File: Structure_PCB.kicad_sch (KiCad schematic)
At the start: 137 parts, among them J10 JST-GH 4Pin, J11 JST-GH 4Pin, J12 JST-GH 4Pin, J6 6620XX236022_662004236022, J9 Conn_02x04_Top_Bottom, K2 FINDER-40.61

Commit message: updated StructurePcB
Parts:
- removed D4, D5, D6: ~, Diode_SMD:D_SOD-123F, symbol Device:D_Schottky
- removed F1: 100 mA, Fuse:Fuse_1206_3216Metric_Pad1.42x1.75mm_HandSolder, symbol Device:Fuse
- removed HS10, HS100, HS101, HS102, HS103, HS104, HS105, HS106, HS107, HS108, HS109, HS11, HS110, HS111, HS112, HS113, HS114, HS115, HS116, HS117, HS118, HS119, HS12, HS120, HS13, HS14, HS15, HS16, HS17, HS18, HS19, HS20, HS21, HS22, HS23, HS24, HS25, HS26, HS27, HS28, HS29, HS30, HS31, HS32, HS33, HS34, HS35, HS36, HS37, HS42, HS43, HS44, HS45, HS46, HS47, HS48, HS49, HS50, HS51, HS52, HS53, HS54, HS55, HS56, HS57, HS58, HS59, HS60, HS61, HS62, HS63, HS64, HS65, HS66, HS67, HS68, HS69, HS70, HS71, HS72, HS73, HS74, HS75, HS76, HS77, HS78, HS79, HS80, HS81, HS82, HS83, HS84, HS85, HS86, HS87, HS88, HS89, HS9, HS90, HS91, HS92, HS93, HS94, HS95, HS96, HS97, HS98, HS99: Heatsink_Pad, Heatsink:würth 5x5 heat pads, symbol Mechanical:Heatsink_Pad
- removed J10, J11, J12: JST-GH 4Pin, Connector_JST:JST_GH_SM04B-GHS-TB_1x04-1MP_P1.25mm_Horizontal, symbol Connector:Conn_01x04_Pin
- removed J6: 6620XX236022_662004236022, stigma:Molex_Micro-Fit_3.0_43045-0400_2x02_P3.00mm_Horizontal, symbol Würth connectors:6620XX236022_662004236022
- removed J9: Conn_02x04_Top_Bottom, Connector_Molex:Molex_Micro-Fit_3.0_43045-0800_2x04_P3.00mm_Horizontal, symbol Connector_Generic:Conn_02x04_Top_Bottom
- removed K2: FINDER-40.61, Relay_THT:Relay_SPDT_Finder_40.61, symbol Relay:FINDER-30.22
- added H20, H21, H22: MountingHole_Pad, Mounting_Wuerth:Mounting_Wuerth_WA-SMSR-3.2mm_H4.6mm_ReverseMount_9775046960, symbol Mechanical:MountingHole_Pad
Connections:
- removed net GND: H1.1, H10.1, H11.1, H12.1, H13.1, H14.1, H15.1, H16.1, H17.1, H18.1, H19.1, H2.1, H3.1, H4.1, H5.1, H6.1, H7.1, H8.1, H9.1
- no-connect marks 0 -> 23
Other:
- note added: "Mounting Arming"
- note removed: "12V ->"
- note removed: "2 in 1 out => power supply for arming (of own PB or other SB for redundancy)"
- note removed: "<- 12V"
- note removed: "<- GND"
- note removed: "GND ->"
- note removed: "PB"
- note removed: "SB"
- note removed: "arming PB"
- note removed: "to arming switch"

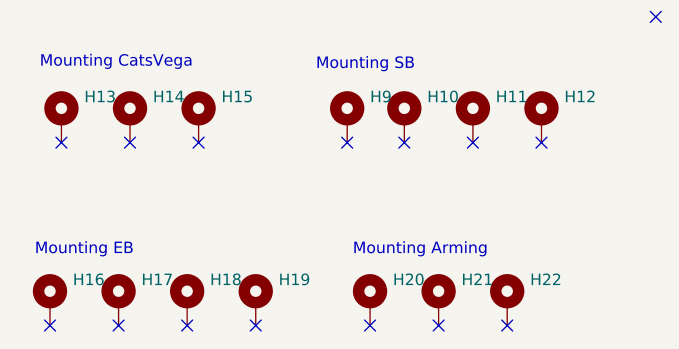
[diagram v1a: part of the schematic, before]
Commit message: Add files via upload
updated the structure PCB to fit Arming and Batteryboard
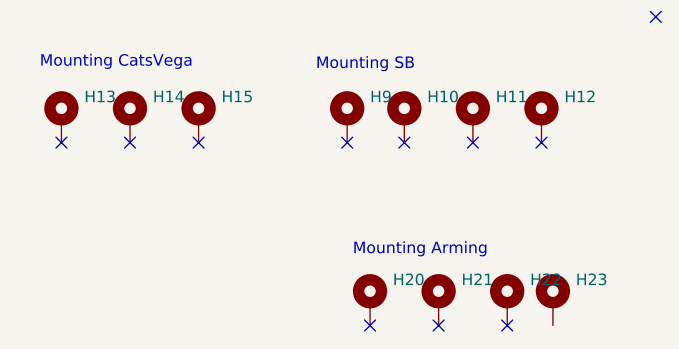
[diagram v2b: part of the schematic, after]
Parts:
- removed H16, H17, H18, H19: MountingHole_Pad, Mounting_Wuerth:Mounting_Wuerth_WA-SMSR-3.2mm_H4.6mm_ReverseMount_9775046960, symbol Mechanical:MountingHole_Pad
- added H23: MountingHole_Pad, Mounting_Wuerth:Mounting_Wuerth_WA-SMSR-3.2mm_H4.6mm_ReverseMount_9775046960, symbol Mechanical:MountingHole_Pad
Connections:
- no-connect marks 23 -> 19
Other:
- note removed: "Mounting EB"

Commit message: changed footprint of armingboard mounting holes
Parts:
- H20, H21, H22, H23: footprint Mounting_Wuerth:Mounting_Wuerth_WA-SMSR-3.2mm_H4.6mm_ReverseMount_9775046960 -> MountingHole:MountingHole_3.2mm_M3_DIN965_Pad_TopBottom
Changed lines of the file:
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@@
 			)
 		)
-		(property "Footprint" "Mounting_Wuerth:Mounting_Wuerth_WA-SMSR-3.2mm_H4.6mm_ReverseMount_9775046960"
+		(property "Footprint" "MountingHole:MountingHole_3.2mm_M3_DIN965_Pad_TopBottom"
 			(at 242.57 76.2 0)
 			(hide yes)
@@
 			)
 		)
-		(property "Footprint" "Mounting_Wuerth:Mounting_Wuerth_WA-SMSR-3.2mm_H4.6mm_ReverseMount_9775046960"
+		(property "Footprint" "MountingHole:MountingHole_3.2mm_M3_DIN965_Pad_TopBottom"
 			(at 255.27 76.2 0)
 			(hide yes)
@@
 			)
 		)
-		(property "Footprint" "Mounting_Wuerth:Mounting_Wuerth_WA-SMSR-3.2mm_H4.6mm_ReverseMount_9775046960"
+		(property "Footprint" "MountingHole:MountingHole_3.2mm_M3_DIN965_Pad_TopBottom"
 			(at 234.95 76.2 0)
 			(hide yes)
@@
 			)
 		)
-		(property "Footprint" "Mounting_Wuerth:Mounting_Wuerth_WA-SMSR-3.2mm_H4.6mm_ReverseMount_9775046960"
+		(property "Footprint" "MountingHole:MountingHole_3.2mm_M3_DIN965_Pad_TopBottom"
 			(at 250.19 76.2 0)
 			(hide yes)

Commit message: improve silkscreen, center fc and fix mounting holes
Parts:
- H20, H21, H22, H23: footprint MountingHole:MountingHole_3.2mm_M3_DIN965_Pad_TopBottom -> Mounting_Wuerth:Mounting_Wuerth_WA-SMSR-3.2mm_H4.6mm_ReverseMount_9775046960
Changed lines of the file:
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@@
 			)
 		)
-		(property "Footprint" "MountingHole:MountingHole_3.2mm_M3_DIN965_Pad_TopBottom"
+		(property "Footprint" "Mounting_Wuerth:Mounting_Wuerth_WA-SMSR-3.2mm_H4.6mm_ReverseMount_9775046960"
 			(at 242.57 76.2 0)
 			(hide yes)
@@
 			)
 		)
-		(property "Footprint" "MountingHole:MountingHole_3.2mm_M3_DIN965_Pad_TopBottom"
+		(property "Footprint" "Mounting_Wuerth:Mounting_Wuerth_WA-SMSR-3.2mm_H4.6mm_ReverseMount_9775046960"
 			(at 255.27 76.2 0)
 			(hide yes)
@@
 			)
 		)
-		(property "Footprint" "MountingHole:MountingHole_3.2mm_M3_DIN965_Pad_TopBottom"
+		(property "Footprint" "Mounting_Wuerth:Mounting_Wuerth_WA-SMSR-3.2mm_H4.6mm_ReverseMount_9775046960"
 			(at 234.95 76.2 0)
 			(hide yes)
@@
 			)
 		)
-		(property "Footprint" "MountingHole:MountingHole_3.2mm_M3_DIN965_Pad_TopBottom"
+		(property "Footprint" "Mounting_Wuerth:Mounting_Wuerth_WA-SMSR-3.2mm_H4.6mm_ReverseMount_9775046960"
 			(at 250.19 76.2 0)
 			(hide yes)
